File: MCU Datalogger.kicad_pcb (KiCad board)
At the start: 4 copper layers, 53.8 x 35.8 mm, 30 parts, among them J1 Conn_01x04_Pin, J2 Conn_01x09_Pin, J3 Conn_01x04_Pin, J4 Conn_02x03_Odd_Even, U1 24LC1025, U2 24LC1025, U3 DS1337S_, U4 ATMEGA328P-AU, Y2 16 MHz

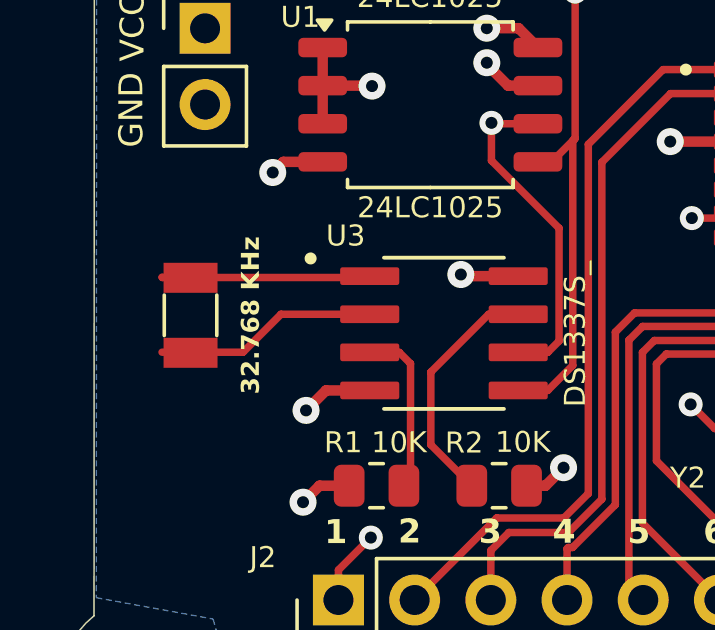
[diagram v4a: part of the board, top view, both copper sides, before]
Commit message: Updated 3215 32.768kHz Oscillator in the 4layer PCB
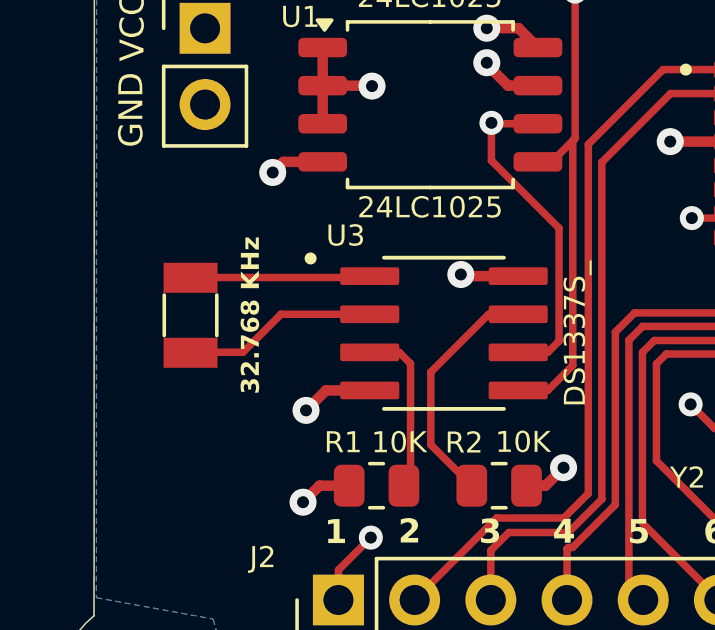
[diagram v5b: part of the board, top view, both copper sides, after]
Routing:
- net Net-(U3-X1): track 6.95 -> 6.00 mm
- net Net-(U3-X2): track 7.45 -> 6.50 mm
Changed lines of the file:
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@@
 			(drillshape 0)
 			(scaleselection 1)
-			(outputdirectory "4_layer_MCU_Datalogger_Gerbers/")
+			(outputdirectory "4_layer_3215Osc_MCU_Datalogger_Gerbers/")
 		)
 	)
@@
 		)
 	)
-	(gr_text "Copper Layer Count: "
-		(at 125.642857 76.94 0)
+	(gr_text "None"
+		(at 155.287143 88.521 0)
 		(layer "User.1")
 		(effects
@@
 		)
 	)
-	(gr_text "53.8097 mm x 35.8235 mm"
-		(at 158.3 80.897 0)
+	(gr_text "0.2000 mm / 0.0000 mm"
+		(at 155.287143 84.564 0)
 		(layer "User.1")
 		(effects
@@
 		)
 	)
-	(gr_text "4"
-		(at 158.3 76.94 0)
+	(gr_text "Castellated pads: "
+		(at 122.63 92.478 0)
 		(layer "User.1")
 		(effects
@@
 		)
 	)
-	(gr_text "0.2000 mm / 0.0000 mm"
-		(at 158.3 84.854 0)
+	(gr_text "No"
+		(at 155.287143 96.435 0)
 		(layer "User.1")
 		(effects
@@
 		)
 	)
-	(gr_text "No"
-		(at 217.399995 92.768 0)
+	(gr_text "Min track/spacing: "
+		(at 122.63 84.564 0)
 		(layer "User.1")
 		(effects
@@
 		)
 	)
-	(gr_text "No"
-		(at 158.3 92.768 0)
+	(gr_text ""
+		(at 189.444281 80.607 0)
 		(layer "User.1")
 		(effects
@@
 		)
 	)
-	(gr_text "No"
-		(at 158.3 96.725 0)
+	(gr_text "Min hole diameter: "
+		(at 189.444281 84.564 0)
 		(layer "User.1")
 		(effects
@@
 		)
 	)
-	(gr_text ""
-		(at 217.399995 80.897 0)
+	(gr_text "53.8097 mm x 35.8235 mm"
+		(at 155.287143 80.607 0)
 		(layer "User.1")
 		(effects
@@
 		)
 	)
-	(gr_text "Board Thickness: "
-		(at 192.457138 76.94 0)
+	(gr_text "Impedance Control: "
+		(at 189.444281 88.521 0)
 		(layer "User.1")
 		(effects
@@
 		)
 	)
-	(gr_text "BOARD CHARACTERISTICS"
-		(at 124.892857 71.446 0)
+	(gr_text "No"
+		(at 214.387138 92.478 0)
 		(layer "User.1")
 		(effects
 			(font
-				(size 2 2)
-				(thickness 0.4)
+				(size 1.5 1.5)
+				(thickness 0.2)
 			)
 			(justify left top)
 		)
 	)
-	(gr_text "Plated Board Edge: "
-		(at 192.457138 92.768 0)
+	(gr_text "BOARD CHARACTERISTICS"
+		(at 121.88 71.156 0)
 		(layer "User.1")
 		(effects
 			(font
-				(size 1.5 1.5)
-				(thickness 0.2)
+				(size 2 2)
+				(thickness 0.4)
 			)
 			(justify left top)
 		)
 	)
-	(gr_text "Edge card connectors: "
-		(at 125.642857 96.725 0)
+	(gr_text "Copper Layer Count: "
+		(at 122.63 76.65 0)
 		(layer "User.1")
 		(effects
@@
 		)
 	)
-	(gr_text "Copper Finish: "
-		(at 125.642857 88.811 0)
+	(gr_text "No"
+		(at 214.387138 88.521 0)
 		(layer "User.1")
 		(effects
@@
 		)
 	)
-	(gr_text "0.3000 mm"
-		(at 217.399995 84.854 0)
+	(gr_text ""
+		(at 214.387138 80.607 0)
 		(layer "User.1")
 		(effects
@@
 	)
 	(gr_text "Board overall dimensions: "
-		(at 125.642857 80.897 0)
+		(at 122.63 80.607 0)
 		(layer "User.1")
 		(effects
@@
 		)
 	)
-	(gr_text ""
-		(at 192.457138 80.897 0)
+	(gr_text "1.6000 mm"
+		(at 214.387138 76.65 0)
 		(layer "User.1")
 		(effects
@@
 		)
 	)
-	(gr_text "1.6000 mm"
-		(at 217.399995 76.94 0)
+	(gr_text "No"
+		(at 155.287143 92.478 0)
 		(layer "User.1")
 		(effects
@@
 		)
 	)
-	(gr_text "Impedance Control: "
-		(at 192.457138 88.811 0)
+	(gr_text "Board Thickness: "
+		(at 189.444281 76.65 0)
 		(layer "User.1")
 		(effects
@@
 		)
 	)
-	(gr_text "Castellated pads: "
-		(at 125.642857 92.768 0)
+	(gr_text "Edge card connectors: "
+		(at 122.63 96.435 0)
 		(layer "User.1")
 		(effects
@@
 		)
 	)
-	(gr_text "Min hole diameter: "
-		(at 192.457138 84.854 0)
+	(gr_text "0.3000 mm"
+		(at 214.387138 84.564 0)
 		(layer "User.1")
 		(effects
@@
 		)
 	)
-	(gr_text "Min track/spacing: "
-		(at 125.642857 84.854 0)
+	(gr_text "Plated Board Edge: "
+		(at 189.444281 92.478 0)
 		(layer "User.1")
 		(effects
@@
 		)
 	)
-	(gr_text "No"
-		(at 217.399995 88.811 0)
+	(gr_text "Copper Finish: "
+		(at 122.63 88.521 0)
 		(layer "User.1")
 		(effects
@@
 		)
 	)
-	(gr_text "None"
-		(at 158.3 88.811 0)
+	(gr_text "4"
+		(at 155.287143 76.65 0)
 		(layer "User.1")
 		(effects
@@
 	)
 	(segment
-		(start 66.52 84.5)
-		(end 73.3875 84.5)
+		(start 67.46 84.51)
+		(end 67.47 84.5)
 		(width 0.25)
 		(layer "F.Cu")
@@
 	)
 	(segment
-		(start 66.51 84.49)
-		(end 66.52 84.5)
+		(start 67.47 84.5)
+		(end 73.3875 84.5)
 		(width 0.25)
 		(layer "F.Cu")
@@
 	)
 	(segment
-		(start 66.51 86.99)
-		(end 69.21 86.99)
+		(start 67.46 87.01)
+		(end 67.48 86.99)
 		(width 0.25)
 		(layer "F.Cu")
@@
 	)
 	(segment
+		(start 67.48 86.99)
+		(end 69.21 86.99)
+		(width 0.25)
+		(layer "F.Cu")
+		(net 25)
+	)
+	(segment
 		(start 79.3675 86.995)
 		(end 79.7435 86.619)
@@
 	)
 	(group "group-boardCharacteristics"
-		(members "11305120-7882-4119-9861-e7303eb5c73b" "1aa4679b-51f2-4735-b3bf-36108bd288c8"
-			"39b94338-7820-4cd5-b912-f26e01bbe584" "425d299f-b74c-472e-a522-83bdfc60c71d"
-			"551088e8-f5d9-424c-b127-8b6b53944c0c" "5f7a6262-9fee-4946-8abb-fcb9e52c2e38"
-			"7cb161f7-b37b-4e38-9098-0ea1d90ac3b5" "80783399-a975-465a-86f2-7d39a1d05a71"
-			"82d8e33c-4786-42bc-9edd-300546bd630a" "8f8b8d48-5b2f-4f94-8cc7-dac57bd7fc70"
-			"95adcb29-3df2-49b2-933a-c4c0de0e17f5" "9cfd2cbf-f94a-4d10-97c2-8b445f5284cc"
-			"9de9990d-e2e2-41bd-88c3-d421128fe2f5" "a131ef8f-a302-456e-a443-cfb097152c96"
-			"a7a26fee-8550-4132-bd85-e049cae88adc" "aa1baa05-3528-40c4-a4a1-008d58381dc4"
-			"abc8844b-f88e-4c44-921f-0f42cdd6c4a3" "bf1c6962-cd14-4154-8ff8-3acfb1517133"
-			"c0f22c98-9b91-47af-9e2a-a5f95af9881f" "d43cb409-86e9-4a2d-961d-61111dd4091a"
-			"dc4a3c92-5211-40d7-8633-bd6c06b7259c" "f2dafa17-e48d-44a1-b7be-c6341befcac4"
-			"fbe6a17c-1d8a-46f5-94d1-7f70ebf17bc7"
+		(members "02499886-5c2e-46d5-b1ee-c930435b6dd2" "0afcc92c-1af5-48dd-8ef8-ae205ce4133b"
+			"165caf33-98ec-4474-a391-203edb5f0433" "1bf1a3ac-f4ad-45d3-94db-c1e4361b527f"
+			"21764251-3db8-48ae-a7d2-d6f2650109f4" "27307c4f-5580-41bd-9329-d55f76bacf29"
+			"2dc18d37-a217-4ee1-9a8b-081cf8d1b3b8" "3aaee93b-39f5-4c74-949e-49a560af4e27"
+			"3d3ed4ef-9586-4bfb-9c9c-8411cc2266f0" "40bde4b3-a0cf-4c65-8763-77c22c97bd16"
+			"50989acf-990c-4662-858d-95413938bb6a" "625e0061-bb26-4d3a-8567-f46666c5e894"
+			"7a72356d-e8e8-4e8d-9c8a-47ca2edb5c60" "87f05720-415c-4aee-b9f6-86a4fc6315c3"
+			"8da453b6-989d-4ab2-ae99-dcbafb0dceb9" "924231e4-73a1-48da-8fad-77d85c52bf9e"
+			"998473c6-d0c4-4603-9c54-8a76e6935c75" "9c88b2b6-f2ba-4b34-aa77-f83bf7b3293c"
+			"cd0a12d6-202a-4134-8a28-00fd05291d24" "e8e9483b-fec5-42e5-9178-6236a28a4df9"
+			"e99e3463-1f68-4942-b4fe-450fc3b793c0" "f0b7d813-bf61-4036-9d54-75b4c0476f7c"
+			"f9c567db-e539-4ab7-aef1-589926a385ca"
 		)
 	)
